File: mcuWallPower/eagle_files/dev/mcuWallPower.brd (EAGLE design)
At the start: 26.5 x 30 mm, 5 parts, among them P1 CR2032, U1 USB-MICROB-SMT5-PIN

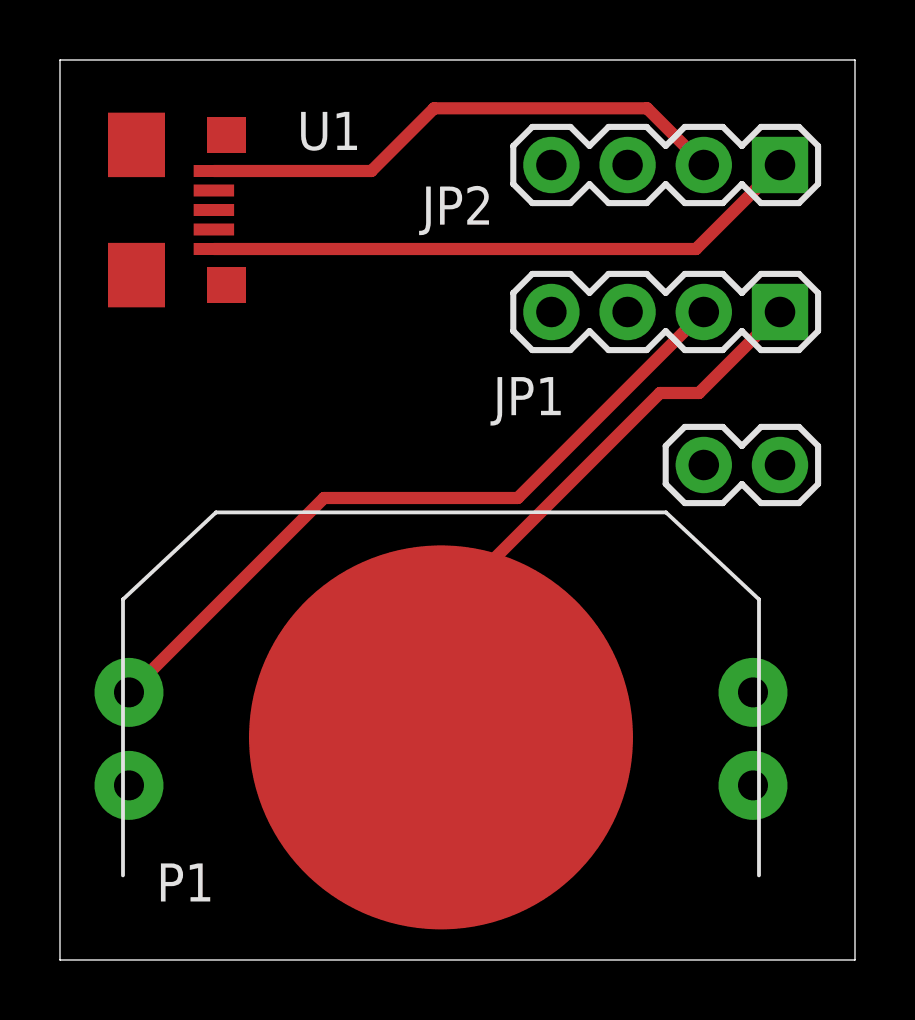
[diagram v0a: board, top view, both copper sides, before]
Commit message: Move components around to make USB micro B power source more stable. Coin battery upright.
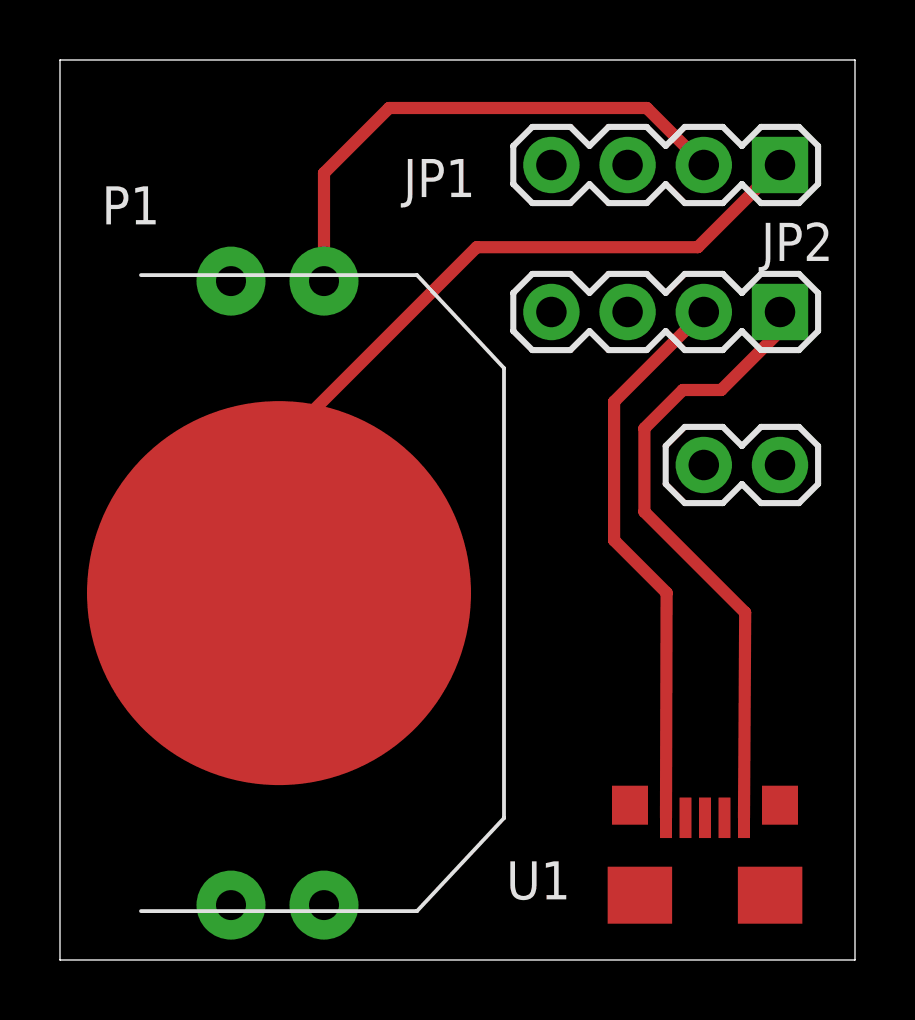
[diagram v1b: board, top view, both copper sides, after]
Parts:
- moved U1 28.3 mm to (21.5, 3.11), turned to 0 degrees
- moved P1 7.23 mm to (7.30, 12.2), turned to 270 degrees
- moved JP1 4.90 mm to (24.0, 26.5)
- moved JP2 4.90 mm to (24.0, 21.6)
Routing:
- net N$1: track 24.4 -> 17.9 mm
- net N$2: track 19.6 -> 25.5 mm
- net N$4: track 18.0 -> 18.8 mm
- net N$3: track 20.0 -> 20.9 mm
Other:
- board text added: "F. Lee 03/10/2014 mcuWallPower R2"
- board text removed: "F. Lee 12/25/2013 mcuWallPower"
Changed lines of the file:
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@@
 <layer number="37" name="tTest" color="7" fill="1" visible="no" active="yes"/>
 <layer number="38" name="bTest" color="7" fill="1" visible="no" active="yes"/>
-<layer number="39" name="tKeepout" color="4" fill="11" visible="yes" active="yes"/>
+<layer number="39" name="tKeepout" color="4" fill="11" visible="no" active="yes"/>
 <layer number="40" name="bKeepout" color="1" fill="11" visible="yes" active="yes"/>
 <layer number="41" name="tRestrict" color="4" fill="10" visible="yes" active="yes"/>
@@
 <wire x1="26.5" y1="30" x2="0" y2="30" width="0" layer="20"/>
 <wire x1="0" y1="30" x2="0" y2="0" width="0" layer="20"/>
-<text x="11.33" y="16.86" size="1" layer="52" rot="MR0">F. Lee
-12/25/2013
-mcuWallPower</text>
+<text x="14.47" y="12.6" size="1" layer="52" rot="MR0">F. Lee
+03/10/2014
+mcuWallPower
+R2</text>
 </plain>
 <attributes>
@@
 </class>
 </classes>
-<designrules name="default">
+<designrules name="LaenPCBOrder">
 <description language="de">&lt;b&gt;EAGLE Design Rules&lt;/b&gt;
 &lt;p&gt;
@@
 Einstellungen hier und speichern die Design Rules unter
 einem neuen Namen ab.</description>
-<description language="en">&lt;b&gt;EAGLE Design Rules&lt;/b&gt;
+<description language="en">&lt;b&gt;Laen's PCB Order Design Rules&lt;/b&gt;
 &lt;p&gt;
-The default Design Rules have been set to cover
-a wide range of applications. Your particular design
-may have different requirements, so please make the
-necessary adjustments and save your customized
-design rules under a new name.</description>
+Please make sure your boards conform to these design rules.</description>
 <param name="layerSetup" value="(1*16)"/>
-<param name="mtCopper" value="0.035mm 0.035mm 0.035mm 0.035mm 0.035mm 0.035mm 0.035mm 0.035mm 0.035mm 0.035mm 0.035mm 0.035mm 0.035mm 0.035mm 0.035mm 0.035mm"/>
-<param name="mtIsolate" value="1.5mm 0.15mm 0.2mm 0.15mm 0.2mm 0.15mm 0.2mm 0.15mm 0.2mm 0.15mm 0.2mm 0.15mm 0.2mm 0.15mm 0.2mm"/>
-<param name="mdWireWire" value="8mil"/>
-<param name="mdWirePad" value="8mil"/>
-<param name="mdWireVia" value="8mil"/>
-<param name="mdPadPad" value="8mil"/>
-<param name="mdPadVia" value="8mil"/>
-<param name="mdViaVia" value="8mil"/>
-<param name="mdSmdPad" value="8mil"/>
-<param name="mdSmdVia" value="8mil"/>
-<param name="mdSmdSmd" value="8mil"/>
+<param name="mtCopper" value="0.0356mm 0.0356mm 0.0356mm 0.0356mm 0.0356mm 0.0356mm 0.0356mm 0.0356mm 0.0356mm 0.0356mm 0.0356mm 0.0356mm 0.0356mm 0.0356mm 0.0356mm 0.0356mm"/>
+<param name="mtIsolate" value="1.5011mm 0.1499mm 0.2007mm 0.1499mm 0.2007mm 0.1499mm 0.2007mm 0.1499mm 0.2007mm 0.1499mm 0.2007mm 0.1499mm 0.2007mm 0.1499mm 0.2007mm"/>
+<param name="mdWireWire" value="6mil"/>
+<param name="mdWirePad" value="6mil"/>
+<param name="mdWireVia" value="6mil"/>
+<param name="mdPadPad" value="6mil"/>
+<param name="mdPadVia" value="6mil"/>
+<param name="mdViaVia" value="6mil"/>
+<param name="mdSmdPad" value="6mil"/>
+<param name="mdSmdVia" value="6mil"/>
+<param name="mdSmdSmd" value="6mil"/>
 <param name="mdViaViaSameLayer" value="8mil"/>
 <param name="mnLayersViaInSmd" value="2"/>
-<param name="mdCopperDimension" value="40mil"/>
-<param name="mdDrill" value="8mil"/>
+<param name="mdCopperDimension" value="15mil"/>
+<param name="mdDrill" value="6mil"/>
 <param name="mdSmdStop" value="0mil"/>
-<param name="msWidth" value="10mil"/>
-<param name="msDrill" value="24mil"/>
-<param name="msMicroVia" value="9.99mm"/>
+<param name="msWidth" value="6mil"/>
+<param name="msDrill" value="13mil"/>
+<param name="msMicroVia" value="13mil"/>
 <param name="msBlindViaRatio" value="0.5"/>
 <param name="rvPadTop" value="0.25"/>
@@
 <param name="rvMicroViaOuter" value="0.25"/>
 <param name="rvMicroViaInner" value="0.25"/>
-<param name="rlMinPadTop" value="10mil"/>
+<param name="rlMinPadTop" value="7mil"/>
 <param name="rlMaxPadTop" value="20mil"/>
-<param name="rlMinPadInner" value="10mil"/>
+<param name="rlMinPadInner" value="7mil"/>
 <param name="rlMaxPadInner" value="20mil"/>
-<param name="rlMinPadBottom" value="10mil"/>
+<param name="rlMinPadBottom" value="7mil"/>
 <param name="rlMaxPadBottom" value="20mil"/>
-<param name="rlMinViaOuter" value="8mil"/>
+<param name="rlMinViaOuter" value="7mil"/>
 <param name="rlMaxViaOuter" value="20mil"/>
-<param name="rlMinViaInner" value="8mil"/>
+<param name="rlMinViaInner" value="7mil"/>
 <param name="rlMaxViaInner" value="20mil"/>
 <param name="rlMinMicroViaOuter" value="4mil"/>
@@
 <param name="mvStopFrame" value="1"/>
 <param name="mvCreamFrame" value="0"/>
-<param name="mlMinStopFrame" value="4mil"/>
-<param name="mlMaxStopFrame" value="4mil"/>
+<param name="mlMinStopFrame" value="3mil"/>
+<param name="mlMaxStopFrame" value="3mil"/>
 <param name="mlMinCreamFrame" value="0mil"/>
 <param name="mlMaxCreamFrame" value="0mil"/>
@@
 </autorouter>
 <elements>
-<element name="P1" library="freddyLibr" package="CR2032/2025" value="CR2032" x="12.7" y="7.42" smashed="yes">
-<attribute name="NAME" x="3.21" y="1.95" size="1.27" layer="25"/>
+<element name="P1" library="freddyLibr" package="CR2032/2025" value="CR2032" x="7.3" y="12.23" smashed="yes" rot="R270">
+<attribute name="NAME" x="1.39" y="24.52" size="1.27" layer="25"/>
 </element>
-<element name="JP1" library="SparkFun-Connectors" package="1X04" value="" x="24" y="21.6" smashed="yes" rot="R180">
-<attribute name="NAME" x="16.8362" y="19.4312" size="1.27" layer="25" ratio="10" rot="R180"/>
+<element name="JP1" library="SparkFun-Connectors" package="1X04" value="" x="24" y="26.5" smashed="yes" rot="R180">
+<attribute name="NAME" x="13.8462" y="26.7012" size="1.27" layer="25" ratio="10" rot="R180"/>
+<attribute name="VALUE" x="25.27" y="29.675" size="1.27" layer="27" rot="R180"/>
+</element>
+<element name="JP3" library="SparkFun-Connectors" package="1X02" value="M02PTH" x="24" y="16.5" smashed="yes" rot="R180"/>
+<element name="JP2" library="SparkFun-Connectors" package="1X04" value="" x="24" y="21.6" smashed="yes" rot="R180">
+<attribute name="NAME" x="25.7762" y="24.5712" size="1.27" layer="25" ratio="10" rot="R180"/>
 <attribute name="VALUE" x="25.27" y="24.775" size="1.27" layer="27" rot="R180"/>
 </element>
-<element name="JP3" library="SparkFun-Connectors" package="1X02" value="M02PTH" x="24" y="16.5" smashed="yes" rot="R180"/>
-<element name="JP2" library="SparkFun-Connectors" package="1X04" value="" x="24" y="26.5" smashed="yes" rot="R180">
-<attribute name="NAME" x="14.4562" y="25.7812" size="1.27" layer="25" ratio="10" rot="R180"/>
-<attribute name="VALUE" x="25.27" y="29.675" size="1.27" layer="27" rot="R180"/>
-</element>
-<element name="U1" library="freddyLibr" package="USB-MICROB-SMT" value="USB-MICROB-SMT5-PIN" x="3.5" y="25" smashed="yes" rot="R270">
-<attribute name="NAME" x="7.9" y="27" size="1.27" layer="25"/>
+<element name="U1" library="freddyLibr" package="USB-MICROB-SMT" value="USB-MICROB-SMT5-PIN" x="21.5" y="3.11" smashed="yes">
+<attribute name="NAME" x="17.02" y="3.29" size="1.27" layer="25" rot="R180"/>
 </element>
 </elements>
@@
 <contactref element="P1" pad="VCC_1"/>
 <contactref element="JP1" pad="2"/>
-<wire x1="2.3" y1="8.92" x2="2.32" y2="8.92" width="0.4064" layer="1"/>
-<wire x1="2.32" y1="8.92" x2="8.8" y2="15.4" width="0.4064" layer="1"/>
-<wire x1="8.8" y1="15.4" x2="15.26" y2="15.4" width="0.4064" layer="1"/>
-<wire x1="15.26" y1="15.4" x2="21.46" y2="21.6" width="0.4064" layer="1"/>
+<wire x1="8.8" y1="22.63" x2="8.8" y2="26.23" width="0.4064" layer="1"/>
+<wire x1="8.8" y1="26.23" x2="10.97" y2="28.4" width="0.4064" layer="1"/>
+<wire x1="10.97" y1="28.4" x2="19.56" y2="28.4" width="0.4064" layer="1"/>
+<wire x1="19.56" y1="28.4" x2="21.46" y2="26.5" width="0.4064" layer="1"/>
 </signal>
 <signal name="N$2">
 <contactref element="P1" pad="GND"/>
 <contactref element="JP1" pad="1"/>
-<wire x1="12.7" y1="7.42" x2="12.7" y2="11.6" width="0.4064" layer="1"/>
-<wire x1="12.7" y1="11.6" x2="20" y2="18.9" width="0.4064" layer="1"/>
-<wire x1="20" y1="18.9" x2="21.3" y2="18.9" width="0.4064" layer="1"/>
-<wire x1="21.3" y1="18.9" x2="24" y2="21.6" width="0.4064" layer="1"/>
+<wire x1="7.3" y1="12.23" x2="7.3" y2="17.17" width="0.4064" layer="1"/>
+<wire x1="7.3" y1="17.17" x2="13.89" y2="23.76" width="0.4064" layer="1"/>
+<wire x1="13.89" y1="23.76" x2="21.26" y2="23.76" width="0.4064" layer="1"/>
+<wire x1="21.26" y1="23.76" x2="24" y2="26.5" width="0.4064" layer="1"/>
 </signal>
 <signal name="N$3">
 <contactref element="JP2" pad="1"/>
 <contactref element="U1" pad="9"/>
-<wire x1="5.13" y1="23.7" x2="21.2" y2="23.7" width="0.4064" layer="1"/>
-<wire x1="21.2" y1="23.7" x2="24" y2="26.5" width="0.4064" layer="1"/>
+<wire x1="24" y1="21.6" x2="24" y2="20.96" width="0.4064" layer="1"/>
+<wire x1="24" y1="20.96" x2="22.04" y2="19" width="0.4064" layer="1"/>
+<wire x1="22.04" y1="19" x2="20.76" y2="19" width="0.4064" layer="1"/>
+<wire x1="20.76" y1="19" x2="19.48" y2="17.72" width="0.4064" layer="1"/>
+<wire x1="19.48" y1="17.72" x2="19.48" y2="14.94" width="0.4064" layer="1"/>
+<wire x1="19.48" y1="14.94" x2="22.84" y2="11.58" width="0.4064" layer="1"/>
+<wire x1="22.84" y1="11.58" x2="22.8" y2="4.74" width="0.4064" layer="1"/>
 </signal>
 <signal name="N$4">
 <contactref element="JP2" pad="2"/>
 <contactref element="U1" pad="5"/>
-<wire x1="5.13" y1="26.3" x2="10.38" y2="26.3" width="0.4064" layer="1"/>
-<wire x1="10.38" y1="26.3" x2="12.47" y2="28.39" width="0.4064" layer="1"/>
-<wire x1="12.47" y1="28.39" x2="19.57" y2="28.39" width="0.4064" layer="1"/>
-<wire x1="19.57" y1="28.39" x2="21.46" y2="26.5" width="0.4064" layer="1"/>
+<wire x1="20.2" y1="4.74" x2="20.22" y2="12.24" width="0.4064" layer="1"/>
+<wire x1="20.22" y1="12.24" x2="18.47" y2="13.99" width="0.4064" layer="1"/>
+<wire x1="18.47" y1="13.99" x2="18.47" y2="18.61" width="0.4064" layer="1"/>
+<wire x1="18.47" y1="18.61" x2="21.46" y2="21.6" width="0.4064" layer="1"/>
 </signal>
 </signals>
